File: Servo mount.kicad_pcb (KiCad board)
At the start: 2 copper layers, 80 x 34.6 mm, 35 parts, among them IC1 ATTINY84-SS, J1 SOLDER_PAD, J2 SOLDER_PAD, J3 SOLDER_PAD, K5 CONN_3, K6 CONN_3, P1 CONN_3X2, Q1 BC847, Q2 BC847, U1 uA78L05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

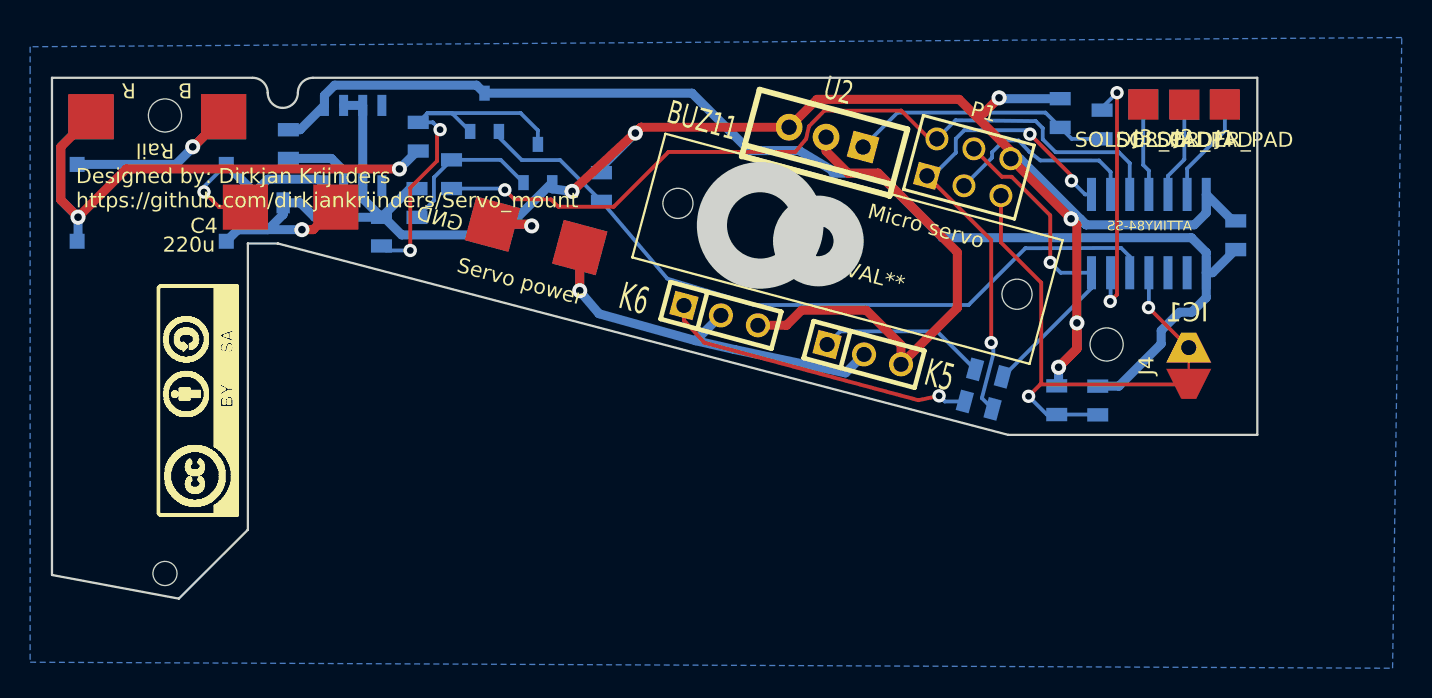
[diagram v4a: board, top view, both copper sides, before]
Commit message: Adapted Board shape to 247?? points
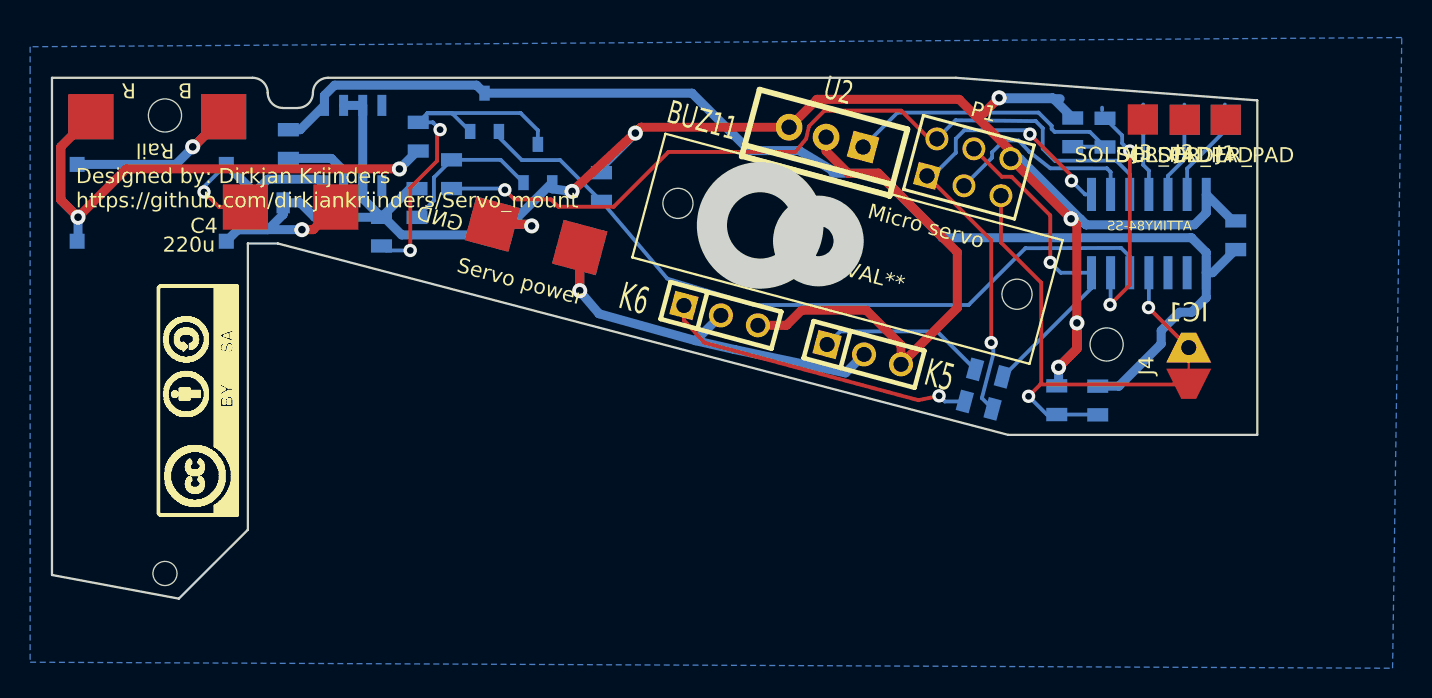
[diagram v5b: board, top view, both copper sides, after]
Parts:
- moved R3 1.53 mm to (167.8, 103.6)
- moved J1 1.02 mm to (177.9, 102.8)
- moved J2 1.01 mm to (175.2, 102.8)
- moved J3 1.00 mm to (172.4, 102.8)
- moved R2 0.57 mm to (169.9, 103.6)
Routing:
- net GND: track 148.5 -> 154.0 mm
- net Net-(R2-Pad2): track 17.5 -> 20.2 mm
- net GND FET: track 17.5 -> 15.7 mm
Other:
- outline, holes or cut-outs redrawn

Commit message: Adepted PCB shape for 24712
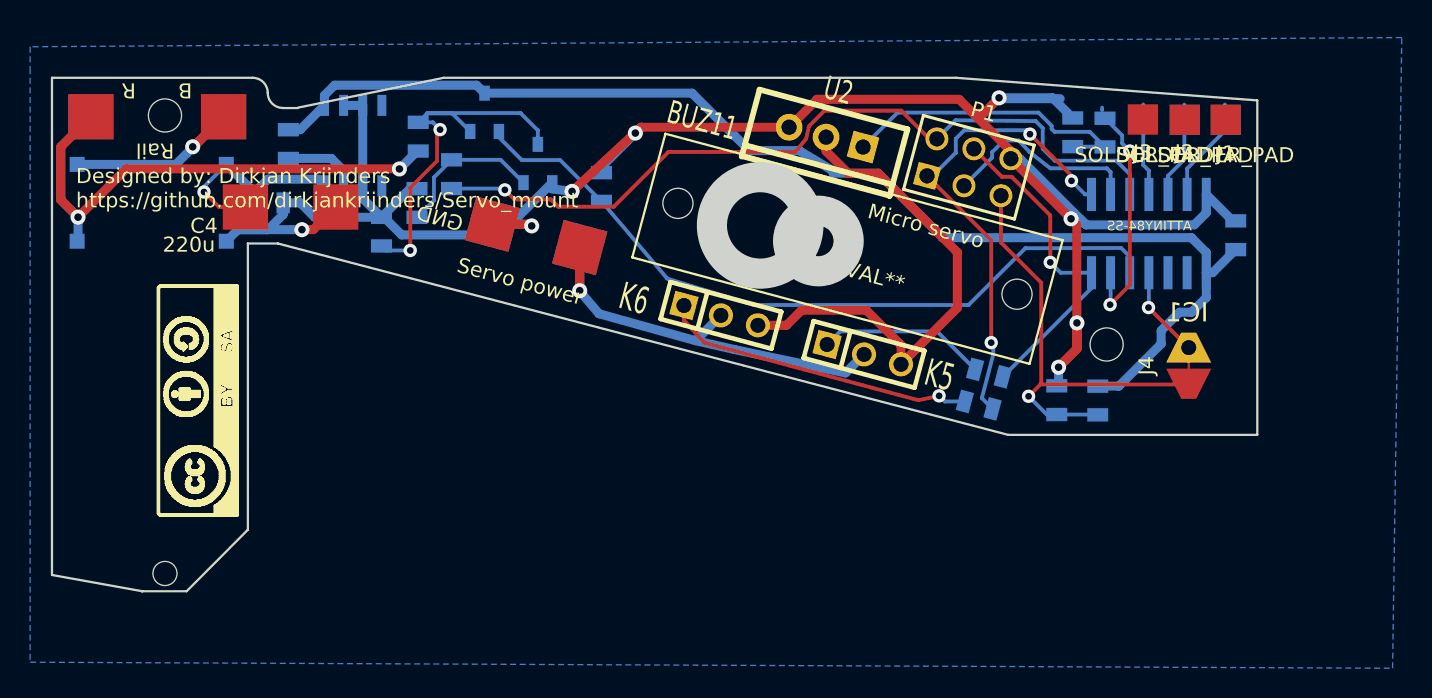
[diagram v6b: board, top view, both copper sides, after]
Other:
- board size 80 x 34.6 mm -> 80 x 34.1 mm

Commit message: Updated shape for 24712, made more GND connections
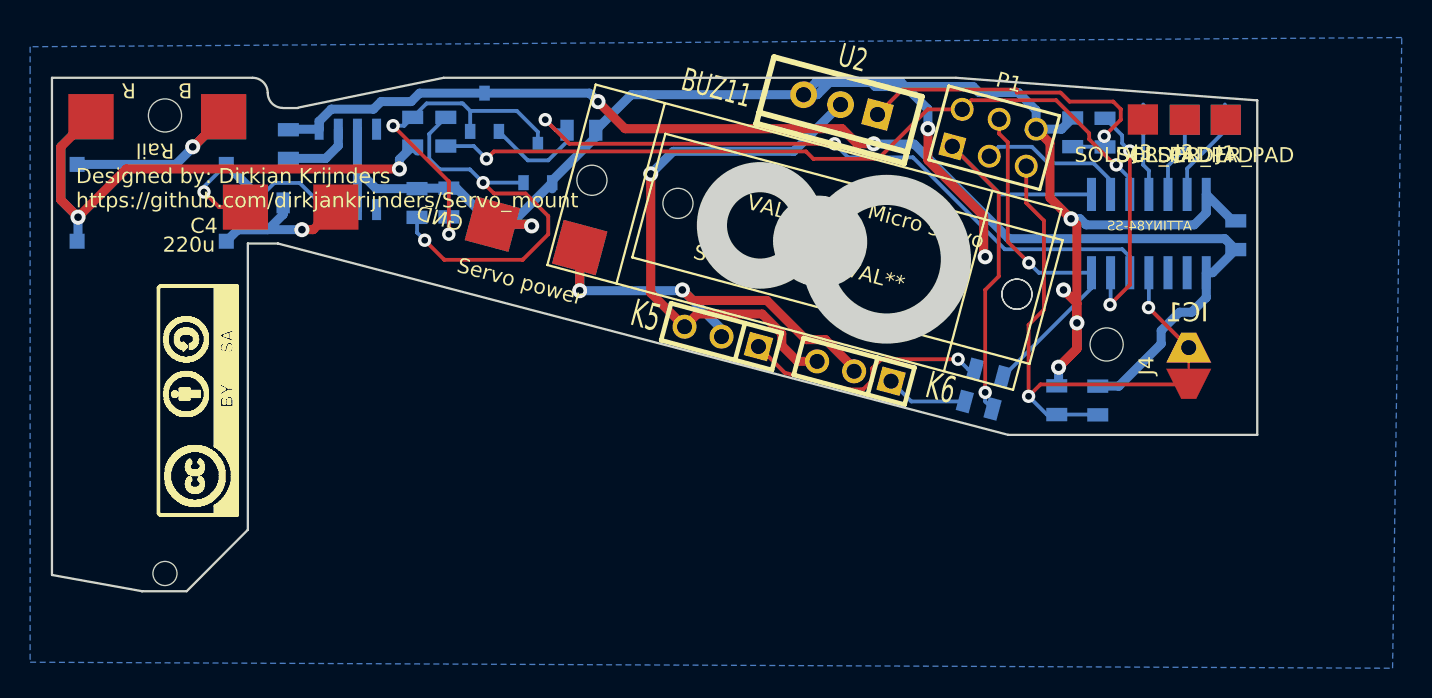
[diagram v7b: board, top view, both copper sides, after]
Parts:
- added SG90_: VAL**, Pyth_servos:Micro_servo_SG90, F.Cu at (149.9, 110.6)
- moved K6 9.59 mm to (153.2, 119.5), turned to 165 degrees
- moved K5 9.53 mm to (144.4, 117.2), turned to 165 degrees
- moved C8 4.87 mm to (126.3, 108.3)
- moved R12 4.00 mm to (135.1, 103.5), turned to 0 degrees
- moved R8 2.85 mm to (126.1, 103.6)
- moved P1 2.58 mm to (162.5, 104.0)
- moved U2 2.36 mm to (152.3, 101.8)
- moved U1 1.62 mm to (119.6, 106.1)
- moved R4 0.50 mm to (123.9, 103.6)
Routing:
- net Net-(Q1-Pad2): track 10.2 -> 27.7 mm, vias 0 -> 2
- net Net-(K6-Pad1): track 21.0 -> 5.45 mm, vias 1 -> 0
- net Net-(K5-Pad1): track 11.2 -> 17.7 mm, vias 0 -> 1
- net GND: track 154.0 -> 148.8 mm
- net Rail signal: track 49.5 -> 53.4 mm, vias 0 -> 2
- net SCK: track 13.5 -> 10.5 mm
- net AGND: track 33.6 -> 36.5 mm, vias 0 -> 1
- net MISO: track 32.4 -> 29.8 mm, vias 3 -> 1
- net Reset: track 29.7 -> 32.3 mm
- net Net-(R2-Pad2): track 20.2 -> 22.6 mm, vias 0 -> 1
- net Net-(C8-Pad1): track 25.5 -> 23.1 mm
- net DIS_SIGNAL: track 53.4 -> 51.2 mm, vias 1 -> 2
- net VCC: track 28.7 -> 30.5 mm, vias 1 -> 2
- net MOSI: track 22.4 -> 24.1 mm
- net Net-(IC1-Pad12): track 6.41 -> 5.41 mm
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
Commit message: Brought out more I/O, option for larger servo
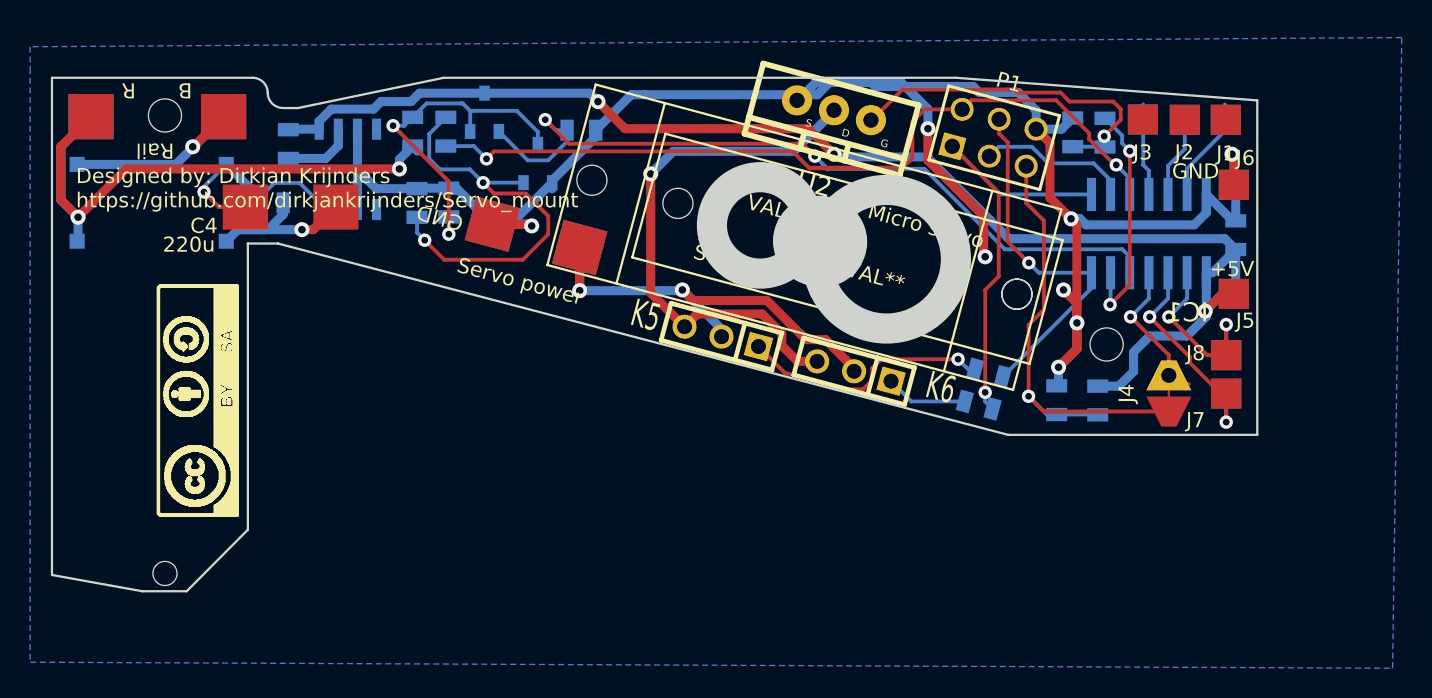
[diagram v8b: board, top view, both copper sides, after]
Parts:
- added J5: +5V, Pyth:solder_pad_2mm_fb, F.Cu at (178.4, 114.3)
- added J6: GND, Pyth:solder_pad_2mm_fb, F.Cu at (178.4, 107.1)
- added J7: SOLDER_PAD, Pyth:solder_pad_2mm_fb, F.Cu at (177.9, 121.0)
- added J8: SOLDER_PAD, Pyth:solder_pad_2mm_fb, F.Cu at (177.9, 118.4)
- U2: footprint TO220_VERT -> Transistors_TO-220:TO-220_FET-GDS_Vertical
- moved J4 2.26 mm to (174.1, 121.0)
- moved U2 0.57 mm to (151.9, 102.2), turned to 165 degrees
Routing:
- net Net-(IC1-Pad3): track 0.00 -> 14.7 mm, vias 0 -> 2
- net Net-(IC1-Pad2): track 0.00 -> 12.4 mm, vias 0 -> 2
- net +5V: track 82.9 -> 91.6 mm, vias 2 -> 3
- net GND: track 148.8 -> 155.4 mm, vias 8 -> 9
- net DIS_SIGNAL: track 51.2 -> 57.1 mm
- net Net-(IC1-Pad4): track 6.09 -> 8.42 mm
- net Reset: track 32.3 -> 31.0 mm
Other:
- outline, holes or cut-outs redrawn
- net class Default: clearance 0.254 -> 0.15
- net class Power: clearance 0.254 -> 0.2
- rule trace_clearance: 0.254 -> 0.15
- rule trace_min: 0.254 -> 0.127
